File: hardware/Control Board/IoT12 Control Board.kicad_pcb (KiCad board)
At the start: 2 copper layers, 99.1 x 69.8 mm, 122 parts, among them J10 USB_B_Micro, J11 Conn_ARM_JTAG_SWD_10, J9 Conn_ARM_JTAG_SWD_10, Q1 MMBT2222, Q2 MMBT2222, Q3 AOD403, SW1 Rotary encoder EC11 Plum 15mm, SW2 SW_Push, U1 ATSAMD21G18A-AU, U2 ADS1115IDGS, U3 INA826AID, U4 INA826AID, U5 LM2596S-ADJ, U6 AT24C32, U7 MAX809S, Y1 32768Hz

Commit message: Start of next iteration.
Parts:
- removed the A2 at (0.00, -15.2)
- removed C1, C2: 6.8pF, Capacitor_SMD:C_0805_2012Metric_Pad1.18x1.45mm_HandSolder
- removed C34, C35, C36, C37, C38: 100nF, Capacitor_SMD:C_0805_2012Metric_Pad1.18x1.45mm_HandSolder
- removed C40, C41: 1uF, Capacitor_SMD:C_0805_2012Metric_Pad1.18x1.45mm_HandSolder
- removed C50: 10uF, Capacitor_SMD:C_0805_2012Metric_Pad1.18x1.45mm_HandSolder
- removed the C60 at (-29.2, -24.1)
- removed C70, C71: 100uF/35V, Capacitor_SMD:CP_Elec_6.3x7.7
- removed the D10 at (0.00, 5.08)
- removed the D4 at (-35.6, -8.89)
- removed D6, D7: SS34, Diode_SMD:D_SMA
- removed F1: *see schematic., Fuse:Fuse_Bourns_MF-RG1000
- removed F2: 0.5A/30V, Fuse:Fuse_Bourns_MF-RG400
- removed J10: USB_B_Micro, Connector_USB-fixed:USB_Micro-B_Amphenol_10118194_Horizontal
- removed J11, J9: Conn_ARM_JTAG_SWD_10, Connector_PinHeader_2.54mm:PinHeader_2x05_P2.54mm_Vertical
- removed J3, J7, J8: ~, TestPoint:TestPoint_THTPad_D2.0mm_Drill1.0mm
- removed L1: 68uH, Inductor-fixed:L_12x12mm_H8mm
- removed L2: 10uH, Inductor_SMD:L_0805_2012Metric_Pad1.15x1.40mm_HandSolder
- removed the Q1 at (2.54, -34.3)
- removed R20: 470R, Resistor_SMD:R_0805_2012Metric_Pad1.20x1.40mm_HandSolder
- removed the R32 at (-2.54, -34.3)
- removed R52: 4k7 1%, Resistor_SMD:R_0805_2012Metric_Pad1.20x1.40mm_HandSolder
- removed R53, R54, R57: 4k7, Resistor_SMD:R_0805_2012Metric_Pad1.20x1.40mm_HandSolder
- removed R83: 1M, Resistor_SMD:R_0805_2012Metric_Pad1.20x1.40mm_HandSolder
- removed REF**: OSHW-Logo_19x20mm_SilkScreen, Symbol:OSHW-Logo_19x20mm_SilkScreen
- removed SW1: Rotary encoder EC11 Plum 15mm, Rotary_Encoder-fixed:RotaryEncoder_Alps_EC11E-Switch_Vertical_H20mm_CircularMountingHoles
- removed SW2: SW_Push, Button_Switch_SMD:SW_SPST_CK_RS282G05A3
- removed TP1, TP10, TP11, TP12, TP13, TP14, TP2, TP3, TP4, TP5, TP6, TP7, TP8, TP9: TestPoint, TestPoint-extra:TestPoint_Pad_D0.75mm
- removed the U5 at (34.3, -8.89)
- removed U6: AT24C32, Package_SO:SOIC-8_3.9x4.9mm_P1.27mm
- removed Y1: 32768Hz, Crystal:Crystal_C26-LF_D2.1mm_L6.5mm_Horizontal_1EP_style1
- added A3: SAMD21_breakout, Module-extra:SAMD21_breakout, F.Cu at (147.3, 85.1)
- added R2: 100R, Resistor_SMD:R_0805_2012Metric_Pad1.20x1.40mm_HandSolder, F.Cu at (186.7, 97.5)
- added R41: 4k7, Resistor_SMD:R_0805_2012Metric_Pad1.20x1.40mm_HandSolder, F.Cu at (120.7, 80.0)
- added R42: 4k7, Resistor_SMD:R_0805_2012Metric_Pad1.20x1.40mm_HandSolder, F.Cu at (124.5, 80.0)
- added R77: 100k, Resistor_SMD:R_0805_2012Metric_Pad1.20x1.40mm_HandSolder, F.Cu at (182.9, 74.9)
- added R78: 100k, Resistor_SMD:R_0805_2012Metric_Pad1.20x1.40mm_HandSolder, F.Cu at (176.5, 70.5)
- added R80: 560k, Resistor_SMD:R_0805_2012Metric_Pad1.20x1.40mm_HandSolder, F.Cu at (125.7, 86.4)
- A1: moved to F.Cu
- C61: value 10uF -> 100uF/35V; footprint Capacitor_SMD:C_0805_2012Metric_Pad1.18x1.45mm_HandSolder -> Capacitor_SMD:CP_Elec_6.3x7.7
- D10: renamed from D9; footprint Diode_SMD:D_SOT-23_ANK -> Package_TO_SOT_SMD:SOT-23
- J1: value ~ -> IDC-Header_2x07_P2.54mm; footprint TestPoint:TestPoint_THTPad_D2.0mm_Drill1.0mm -> Connector_IDC:IDC-Header_2x07_P2.54mm_Vertical; moved to F.Cu
- J2: value ~ -> JST B2B-XH-A; footprint TestPoint:TestPoint_THTPad_D2.0mm_Drill1.0mm -> Connector_JST:JST_XH_B2B-XH-A_1x02_P2.50mm_Vertical; moved to F.Cu
- J4: value ~ -> JST B4B-XH-A; footprint TestPoint:TestPoint_THTPad_D2.0mm_Drill1.0mm -> Connector_JST:JST_XH_B4B-XH-A_1x04_P2.50mm_Vertical; moved to F.Cu
- J5: value ~ -> JST B5B-XH-A; footprint TestPoint:TestPoint_THTPad_D2.0mm_Drill1.0mm -> Connector_JST:JST_XH_B5B-XH-A_1x05_P2.50mm_Vertical; moved to F.Cu
- J6: value ~ -> JST B6B-XH-A; footprint TestPoint:TestPoint_THTPad_D2.0mm_Drill1.0mm -> Connector_JST:JST_XH_B6B-XH-A_1x06_P2.50mm_Vertical; moved to F.Cu
- NT1: footprint NetTie-extra:NetTie-2_SMD_Pad0.25mm -> NetTie-extra:NetTie-2_SMD_Pad0.5mm
- NT2: renamed from NT4; footprint NetTie-extra:NetTie-2_SMD_Pad0.25mm -> NetTie-extra:NetTie-2_SMD_Pad0.5mm
- NT3: renamed from NT5; footprint NetTie-extra:NetTie-2_SMD_Pad0.25mm -> NetTie-extra:NetTie-2_SMD_Pad0.5mm
- R40: value 3k3 -> 4k7 1%
- R73: value 100K -> 100k
- R74: renamed from R80; value 1M -> 100k
- R75: renamed from R81; value 1M -> 100k
- R76: renamed from R82; value 1M -> 100k
- U1: value ATSAMD21G18A-AU -> W25Q64FVSSIG; footprint Package_QFP:TQFP-48_7x7mm_P0.5mm -> Package_SO-fixed:SOIC-8_5.23x5.23mm_P1.27mm
- U3, U4: footprint Package_SO:SOIC-8_3.9x4.9mm_P1.27mm -> Package_SO:MSOP-8_3x3mm_P0.65mm
- moved A1 259.6 mm to (188.0, 91.4)
- moved C60 252.2 mm to (190.5, 77.5), turned to 90 degrees
- moved D3 252.2 mm to (186.7, 102.6), turned to -90 degrees
- moved R43 251.4 mm to (182.9, 121.9)
- moved R44 242.7 mm to (175.3, 121.9)
- moved C32 240.2 mm to (175.3, 110.5), turned to 0 degrees
- moved U2 234.8 mm to (175.3, 104.1), turned to -90 degrees
- moved NT1 234.8 mm to (175.7, 103.8), turned to 90 degrees
- moved R47 230.0 mm to (175.3, 97.8), turned to 0 degrees
- moved U5 225.2 mm to (184.8, 110.5), turned to -90 degrees
- moved C30 223.2 mm to (167.6, 110.5), turned to 0 degrees
- moved R10 221.0 mm to (167.6, 108.0), turned to 0 degrees
- moved R73 219.9 mm to (184.8, 106.7), turned to 0 degrees
- moved J1 219.1 mm to (165.1, 123.7)
- moved U1 215.9 mm to (176.5, 74.9), turned to 180 degrees
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- renumbered A3 to A2, C73 to C60, D11 to D20, D5 to D30, D12 to D4, D8 to D40, Q2 to Q1, Q3 to Q10, R34 to R32, R55 to R43, R56 to R44, R50 to R47, R51 to R48, R58 to R49, R59 to R50, U7 to U5
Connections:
- A1 pad 1: +3V3 -> +3.3V
- A1 pad 12: Net-(A1-Pad12) -> I2S_GAIN1
- A1 pad 13: Net-(A1-Pad13) -> unconnected-(A1-Pad13)
- A1 pad 15: Net-(A1-Pad15) -> I2S_GAIN0
- A1 pad 23: Net-(A1-Pad23) -> TFT_~{CS}
- A1 pad 24: LCD_~{RST} -> TFT_D~{C}
- A1 pad 26: LCD_DATA-~{CMD} -> TFT_~{RST}
- A1 pad 27: ROT_A -> unconnected-(A1-Pad27)
- A1 pad 28: ROT_B -> unconnected-(A1-Pad28)
- A1 pad 29: LCD_~{CE} -> TOUCH_~{CS}
- A1 pad 30: LCD_CLK -> TFT_SCLK
- A1 pad 31: unconnected-(A1-Pad31) -> TFT_MISO
- A1 pad 37: LCD_DIN -> TFT_MOSI
- A1 pad 5: unconnected-(A1-Pad5) -> TOUCH_~{IRQ}
- A1 pad 7: LCD_LED -> TFT_LED
- A1 pad 8: ROT_SW -> I2S_SD
- A2 pad 5: I2S_SD -> Net-(A2-Pad5)
- A2 pad 8: unconnected-(A3-Pad8) -> Net-(A2-Pad8)
- A2 pad 9: unconnected-(A3-Pad9) -> Net-(A2-Pad9)
- C10 pad 1: AIN_COMP -> SHAKE
- C32 pad 1: +3V3 -> +3.3V
- C33 pad 1: /Power/24V_DC_SW -> +3.3V
- C60 pad 1: +3V3 -> +3.3V
- C61 pad 1: +3.3VA -> +5V
- D10 pad 1: +24V -> /Output/GATE
- D10 pad 2: /Output/GATE -> unconnected-(D10-Pad2)
- D3 pad 1: GND -> Net-(D3-Pad1)
- D3 pad 2: +3V3 -> unconnected-(D3-Pad2)
- D3 pad 3: /Brain/USB+ -> Net-(D3-Pad3)
- D4 pad 3: Net-(D12-Pad3) -> Net-(D3-Pad3)
- H1 pad 1: (no net) -> unconnected-(H1-Pad1)
- H2 pad 1: (no net) -> unconnected-(H2-Pad1)
- H3 pad 1: (no net) -> unconnected-(H3-Pad1)
- H4 pad 1: (no net) -> unconnected-(H4-Pad1)
- J1 pad 1: Net-(J1-Pad1) -> +3.3V
- J2 pad 1: Net-(J2-Pad1) -> Net-(A2-Pad9)
- J4 pad 1: /Output/IRON_- -> +24V
- J5 pad 1: IRON_+ -> SHAKE_IN
- J6 pad 1: /Power/24V_DC -> EXP_D5
- R10 pad 2: +3V3 -> +3.3V
- R11 pad 2: +3V3 -> +3.3V
- R31 pad 1: GND -> 24V_ON
- R31 pad 2: Net-(R31-Pad2) -> Net-(J4-Pad4)
- R40 pad 1: +5V -> GND
- R40 pad 2: Net-(R31-Pad2) -> VIN
- R43 pad 2: +3V3 -> +3.3V
- R44 pad 2: +3V3 -> +3.3V
- R47 pad 2: +3V3 -> +3.3V
- R48 pad 2: Net-(J2-Pad1) -> NTC_IN
- R64 pad 1: +3V3 -> +3.3V
- R64 pad 2: Net-(J2-Pad1) -> NTC_IN
- R73 pad 1: Net-(D12-Pad3) -> Net-(D3-Pad3)
- R74 pad 1: +3V3 -> +3.3V
- R74 pad 2: AIN_COMP -> SHAKE
- R75 pad 1: AIN_COMP -> SHAKE
- R75 pad 2: Net-(J1-Pad1) -> SHAKE_IN
- U1 pad 1: /Brain/XIN32 -> FLASH_~{CS}
- U1 pad 2: /Brain/XOUT32 -> MISO
- U1 pad 3: NTC -> +3.3V
- U1 pad 4: /Brain/AREF -> GND
- U1 pad 5: GND -> MOSI
- U1 pad 6: +3.3VA -> SCK
- U1 pad 7: TEMP -> +3.3V
- U1 pad 8: AIN_COMP -> +3.3V
- U2 pad 8: +3V3 -> +3.3V
- U5 pad 2: Net-(D12-Pad3) -> Net-(D3-Pad3)
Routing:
- net +3.3V: track 0.00 -> 281.0 mm, vias 0 -> 10
- net +3V3: track 258.3 -> 0.00 mm, vias 23 -> 0
- net LCD_DIN: track 97.7 -> 0.00 mm, vias 4 -> 0
- net EXP_D5: track 0.00 -> 87.6 mm, vias 0 -> 3
- net EXP_D7: track 0.00 -> 71.7 mm, vias 0 -> 1
- net TOUCH_~{IRQ}: track 0.00 -> 71.4 mm, vias 0 -> 2
- net ESP32_~{RESET}: track 76.6 -> 6.95 mm
- net LCD_~{CE}: track 69.4 -> 0.00 mm, vias 6 -> 0
- net AIN_COMP: track 68.3 -> 0.00 mm, vias 9 -> 0
- net LCD_CLK: track 67.9 -> 0.00 mm, vias 2 -> 0
- net /Brain/USB+: track 67.1 -> 0.00 mm, vias 3 -> 0
- net ROT_SW: track 66.1 -> 0.00 mm, vias 2 -> 0
- net /Brain/USB-: track 65.7 -> 0.00 mm, vias 5 -> 0
- net HEAT_~{RESET}: track 62.5 -> 0.00 mm, vias 4 -> 0
- net 24V_ON: track 0.00 -> 62.3 mm, vias 0 -> 3
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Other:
- board size 99.1 x 69.8 mm -> 99.1 x 69.9 mm
- board text added: "+24V"
- board text added: "+24V ON"
- board text added: "+5V"
- board text added: "3V3"
- board text added: "D11/SDA"
- board text added: "D13/SCL"
- board text added: "D5"
- board text added: "D7"
- board text added: "ESD, green"
- board text added: "Expansion"
- board text added: "ILI9341 TFT Touch Display"
- board text added: "IoT12 Control Board, 2022-12-20, V2.2, Apache License, Version 2.0 https://github.com/atoomnetmarc/IoT12"
- board text added: "MAX98357 I2S module"
- board text added: "NTC, white"
- board text added: "Power"
- board text added: "SHAKE, blue"
- board text added: "Speaker"
- board text added: "T12"
- board text added: "T12+, red"
- board text added: "T12-, black"
- board text removed: "- SPK +"
- board text removed: "0x48"
- board text removed: "1"
- board text removed: "1, SHAKE"
- board text removed: "1, blue, shake"
- board text removed: "2, NTC"
- board text removed: "2, white, NTC"
- board text removed: "24V max"
- board text removed: "3, ESD"
- board text removed: "3, green, ESD"
- board text removed: "4, T12-"
- board text removed: "4, black, T12-"
- board text removed: "5, T12+"
- board text removed: "5, red, T12+"
- board text removed: "CE"
- board text removed: "CLK"
- board text removed: "D0"
- board text removed: "D1"
- board text removed: "D10"
- board text removed: "D9"
- board text removed: "DC"
- board text removed: "DIN"
- board text removed: "EARTH"
- board text removed: "IoT12, 2021-09-26, V2.1 https://atoomnet.net"
- board text removed: "JTAG ESP32"
- board text removed: "LED"
- board text removed: "MAX98357 module"
- board text removed: "Power supply suggestions: 12V@1.5A (18W) 15V@1.9A (28W) 19V@2.4A (45W) 24V@3.0A (72W)"
- board text removed: "RESET SAMD21"
- board text removed: "RST"
- board text removed: "SWD SAMD21"
- board text removed: "USB SAMD21"
- board text removed: "https://github.com/atoomnetmarc/IoT12-hardware Apache License, Version 2.0"

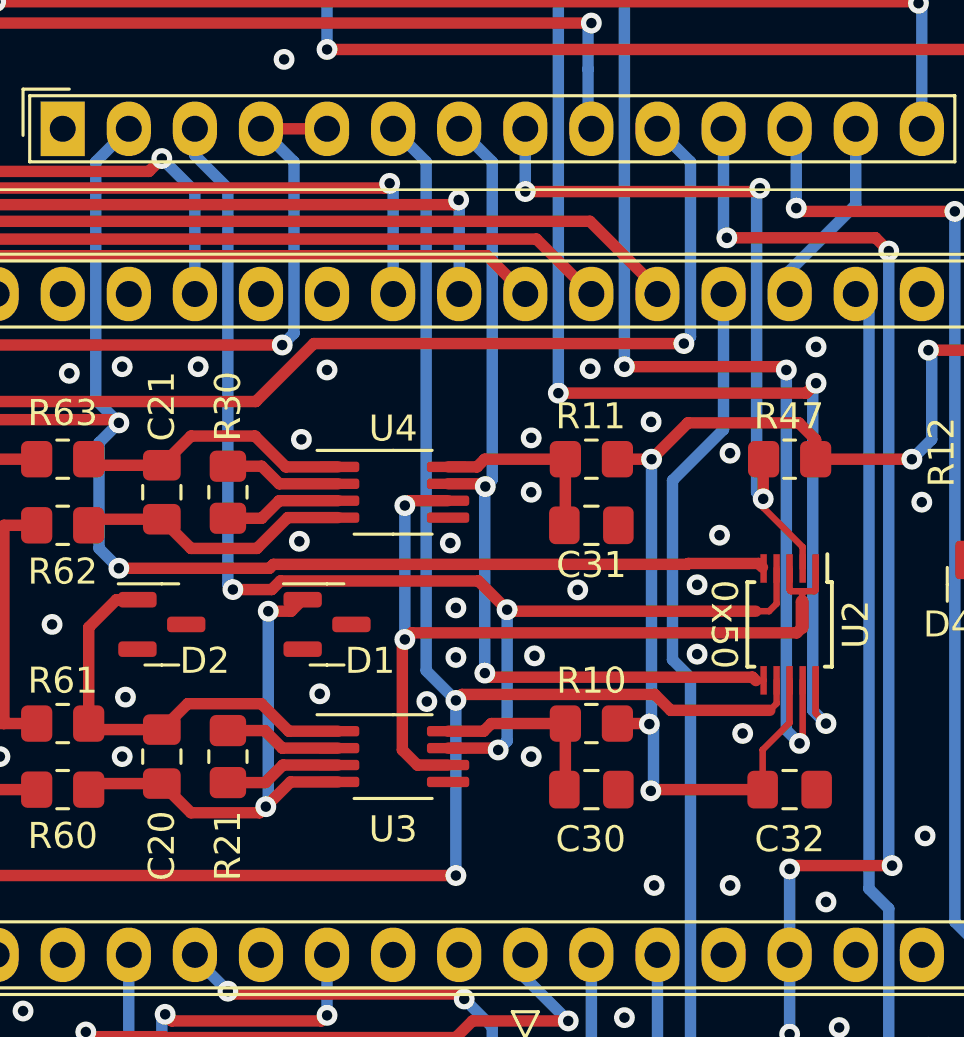
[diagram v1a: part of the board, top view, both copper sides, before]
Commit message: Corrected footprint for INA826AID.
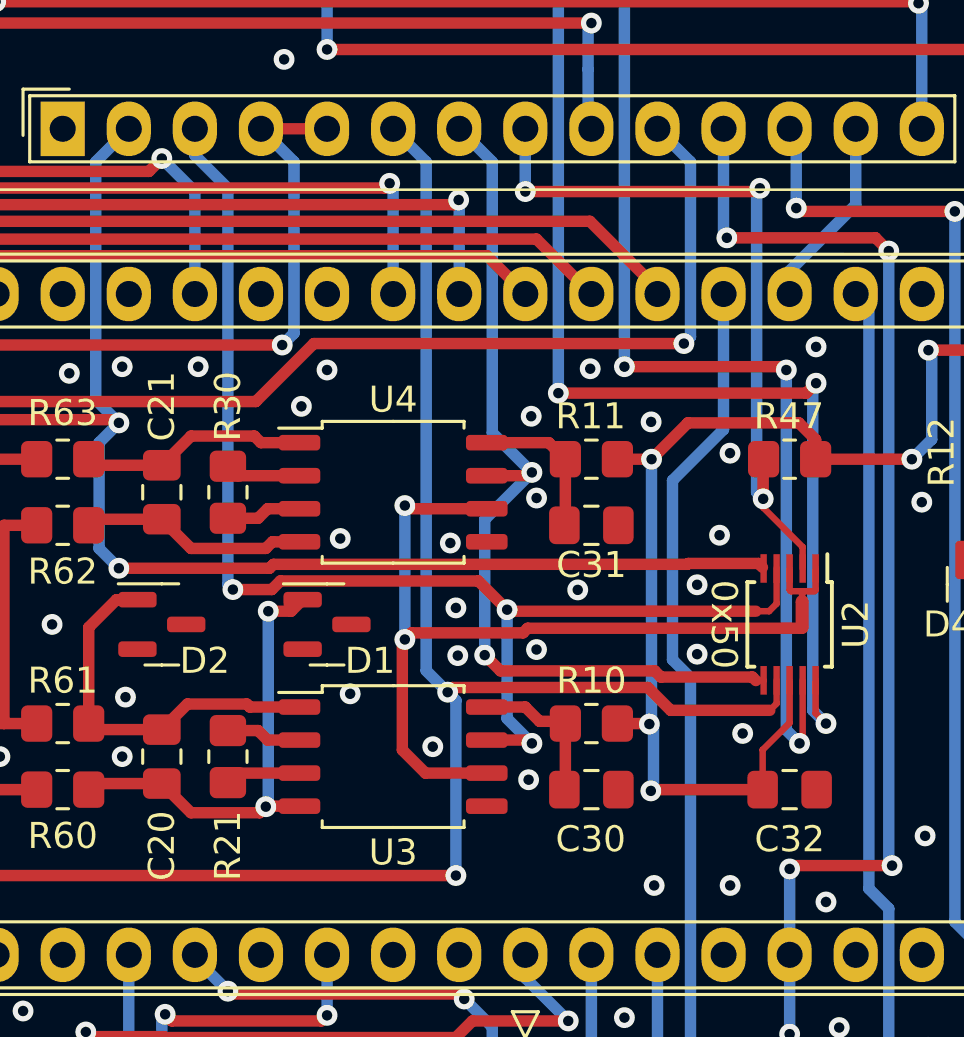
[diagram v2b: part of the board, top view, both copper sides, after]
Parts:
- U3, U4: footprint Package_SO:MSOP-8_3x3mm_P0.65mm -> Package_SO-fixed:SOIC-8_5.23x5.23mm_P1.27mm
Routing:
- net NEAR_ADC_GND: track 28.6 -> 31.7 mm
- net Net-(C20-Pad2): track 16.5 -> 14.7 mm
- net Net-(C20-Pad1): track 19.7 -> 17.8 mm
- net Net-(C21-Pad1): track 10.6 -> 8.77 mm
- net Net-(C21-Pad2): track 10.6 -> 8.77 mm
- net Net-(R30-Pad2): track 4.52 -> 2.90 mm
- net Net-(R21-Pad1): track 4.52 -> 2.90 mm
- net Net-(R21-Pad2): track 4.52 -> 2.90 mm
- net Net-(R30-Pad1): track 4.52 -> 2.90 mm
- net Net-(C30-Pad1): track 7.19 -> 5.84 mm
- net Net-(C31-Pad1): track 7.19 -> 5.84 mm
- net IRON_CURRENT: track 33.9 -> 35.1 mm

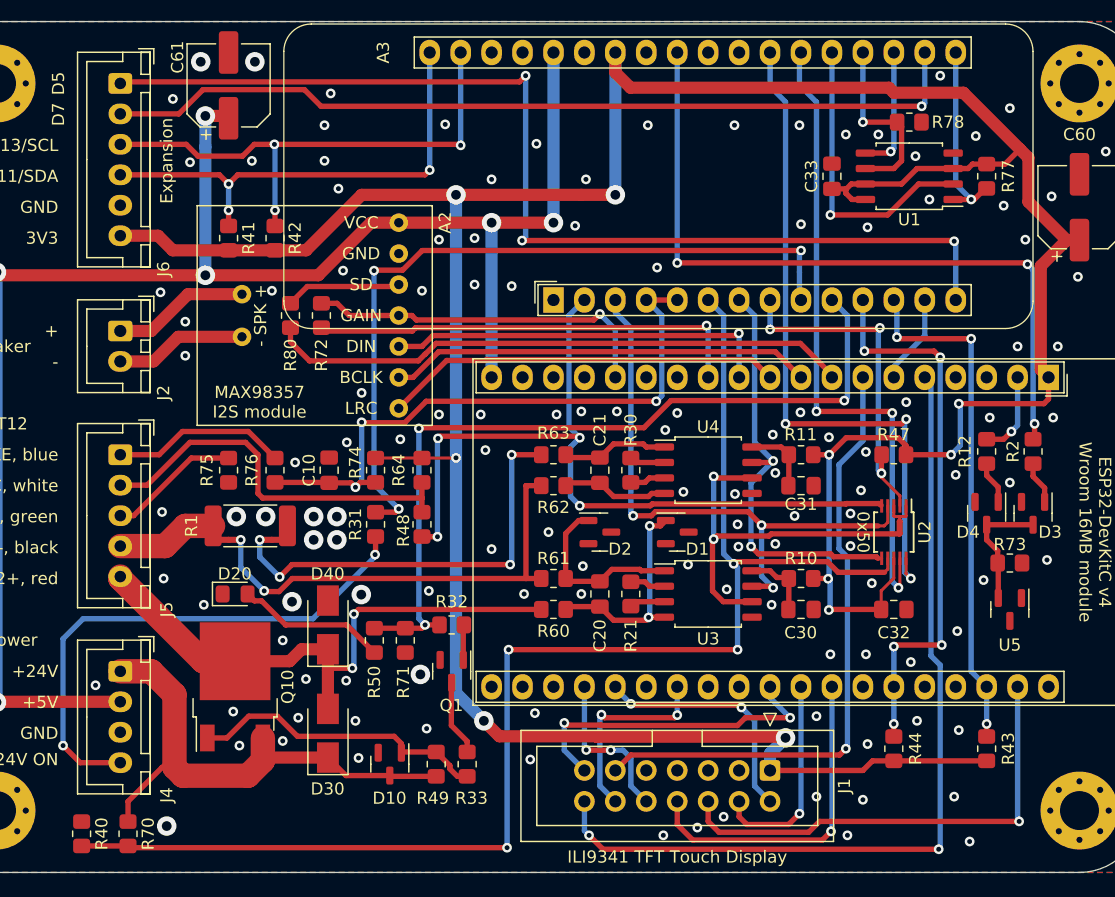
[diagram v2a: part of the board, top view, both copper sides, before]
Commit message: Update Control Board project to Kicad 7.0.2
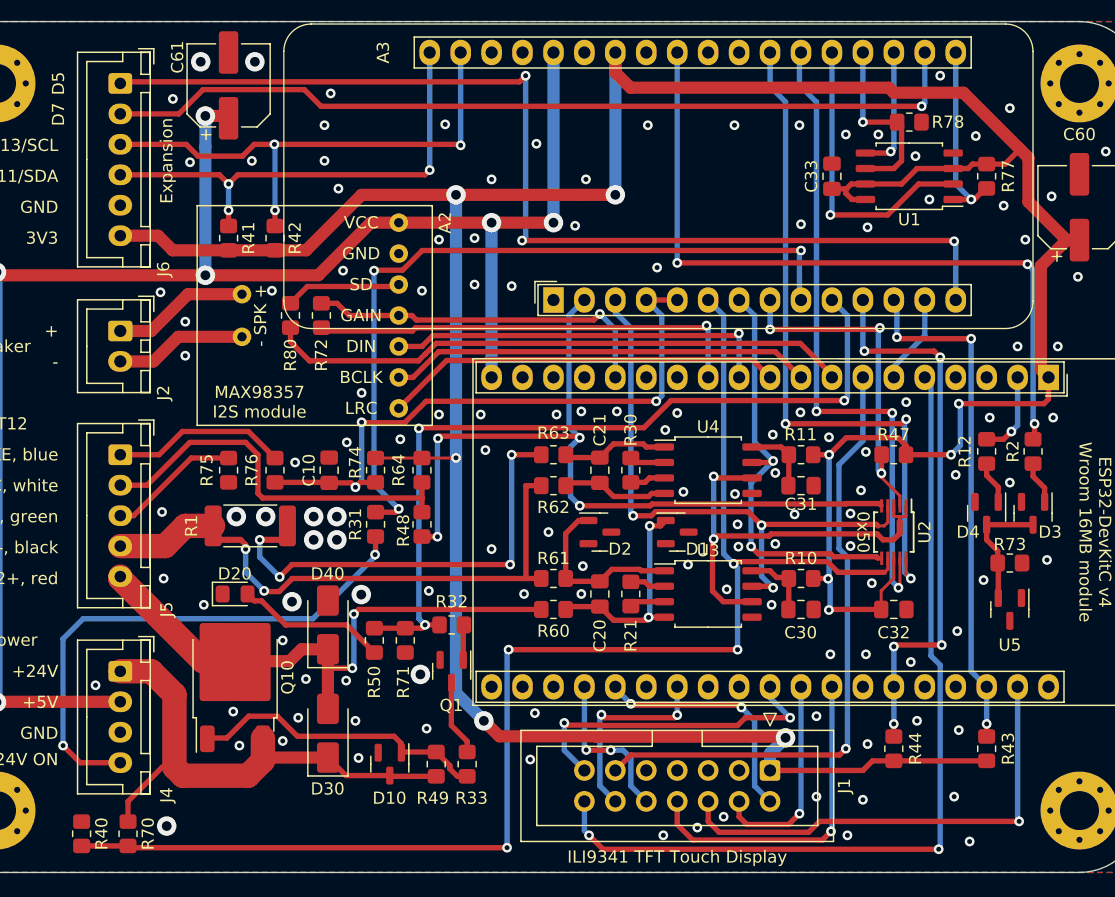
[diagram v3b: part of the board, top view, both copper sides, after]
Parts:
- moved Q10 0.77 mm to (121.2, 116.1)
